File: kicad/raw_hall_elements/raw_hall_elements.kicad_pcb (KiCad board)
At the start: 2 copper layers, 23 parts, among them J1 Conn_01x03_Socket, J2 Conn_01x02_Socket, U1 MCP6022

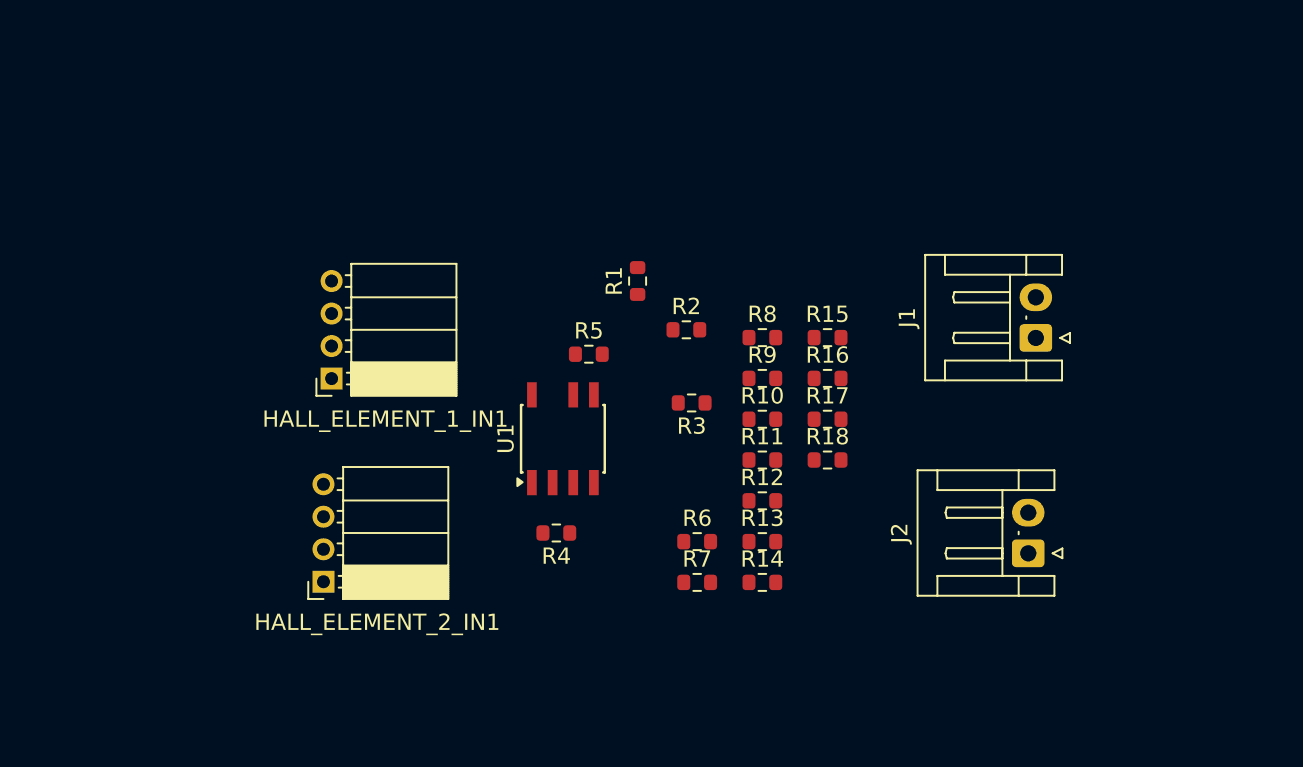
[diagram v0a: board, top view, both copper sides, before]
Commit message: Schematic now uses smaller opamp
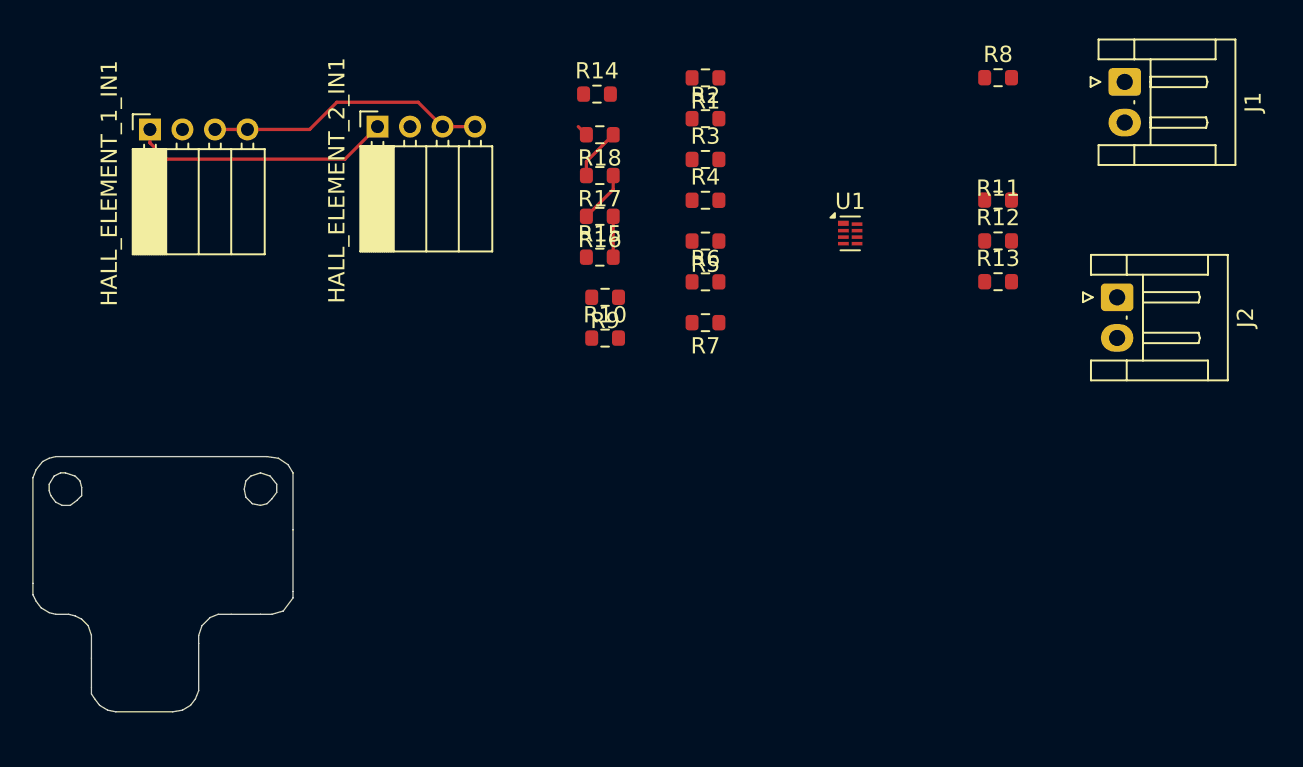
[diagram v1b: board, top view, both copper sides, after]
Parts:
- U1: value MCP6022 -> LMV358; footprint Package_SO:SOIC-8-N7_3.9x4.9mm_P1.27mm -> Package_DFN_QFN:OnSemi_UDFN-8_1.2x1.8mm_P0.4mm
- moved R14 31.7 mm to (136.0, 49.5)
- moved HALL_ELEMENT_2_IN1 28.2 mm to (122.5, 51.5), turned to 90 degrees
- moved R18 24.4 mm to (136.2, 52.0), turned to 180 degrees
- moved R4 22.4 mm to (142.7, 56.0), turned to 0 degrees
- moved U1 21.7 mm to (151.6, 58.1), turned to 0 degrees
- moved R11 21.6 mm to (160.7, 56.0)
- moved R13 21.6 mm to (160.7, 61.0)
- moved R8 21.6 mm to (160.7, 48.5)
- moved R12 21.6 mm to (160.7, 58.5)
- moved R17 20.5 mm to (136.2, 54.5), turned to 180 degrees
- moved HALL_ELEMENT_1_IN1 19.0 mm to (108.5, 51.7), turned to 90 degrees
- moved R16 17.2 mm to (136.2, 57.0), turned to 180 degrees
- moved J1 16.7 mm to (168.5, 48.8), turned to -90 degrees
- moved J2 16.7 mm to (168.0, 62.0), turned to -90 degrees
- moved R6 16.0 mm to (142.7, 61.0)
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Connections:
- R13 pad 1: Net-(R13-Pad1) -> Hall1_out+
- R16 pad 1: Net-(R15-Pad2) -> Hall2_out+
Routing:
- net Vin-: track 0.00 -> 18.0 mm
- net Vin+: track 0.00 -> 16.1 mm
- net Hall2_adj+: track 0.00 -> 3.19 mm
- net Net-(R17-Pad2): track 0.00 -> 3.19 mm
- net Net-(R15-Pad2): track 0.00 -> 2.51 mm
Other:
- board outline added: 16 x 15.7 mm
- board text added: "For Instructional Use Only."
- board text added: "SOLIDWORKS Educational Product."

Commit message: more progress
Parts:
- removed HALL_ELEMENT_1_IN1, HALL_ELEMENT_2_IN1: Conn_01x04, Connector_PinSocket_2.00mm:PinSocket_1x04_P2.00mm_Horizontal
- removed J1: Conn_01x03_Socket, Connector_JST:JST_EH_S2B-EH_1x02_P2.50mm_Horizontal
- removed J2: Conn_01x02_Socket, Connector_JST:JST_EH_S2B-EH_1x02_P2.50mm_Horizontal
- removed R12, R18: 1.5k, Resistor_SMD:R_0603_1608Metric
- removed R14, R15: 200, Resistor_SMD:R_0603_1608Metric
- added 3V3: Conn_01x01, TestPoint:TestPoint_THTPad_1.0x1.0mm_Drill0.5mm, F.Cu at (105.5, 73.0)
- added 5V1: Conn_01x01, TestPoint:TestPoint_THTPad_1.0x1.0mm_Drill0.5mm, F.Cu at (107.5, 73.0)
- added GND1: Conn_01x01, TestPoint:TestPoint_THTPad_1.0x1.0mm_Drill0.5mm, F.Cu at (109.5, 73.0)
- added IC1: AHE300G-PA4-B, KiCad:AHE300GPA4B, F.Cu at (103.0, 80.2)
- added IC2: AHE300G-PA4-B, KiCad:AHE300GPA4B, F.Cu at (112.5, 80.0)
- added VO1: Conn_01x01, TestPoint:TestPoint_THTPad_1.0x1.0mm_Drill0.5mm, F.Cu at (106.0, 86.5)
- added VO2: Conn_01x01, TestPoint:TestPoint_THTPad_1.0x1.0mm_Drill0.5mm, F.Cu at (110.0, 86.5)
- moved R8 61.6 mm to (105.8, 76.5)
- moved R13 54.7 mm to (109.2, 79.5)
- moved R11 49.5 mm to (115.2, 75.5)
- moved U1 46.8 mm to (108.9, 77.4), turned to 90 degrees
- moved R3 42.5 mm to (106.0, 75.0)
- moved R6 42.4 mm to (102.8, 75.5)
- moved R7 42.1 mm to (102.8, 77.0), turned to 0 degrees
- moved R17 41.6 mm to (106.3, 83.5), turned to 0 degrees
- moved R1 38.8 mm to (112.2, 72.5), turned to 0 degrees
- moved R4 38.4 mm to (109.3, 75.0)
- moved R2 38.2 mm to (112.2, 74.0)
- moved R16 37.4 mm to (109.8, 83.5), turned to 0 degrees
- moved R5 34.8 mm to (112.3, 75.5), turned to 0 degrees
- moved R9 28.5 mm to (112.3, 77.0), turned to 0 degrees
- moved R10 24.6 mm to (115.3, 77.0)
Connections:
- R11 pad 2: Net-(R11-Pad2) -> Vin-
- R17 pad 2: Net-(R17-Pad2) -> Vin-
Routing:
- net Vin-: track 18.0 -> 0.00 mm
- net Vin+: track 16.1 -> 0.00 mm
- net Hall2_adj+: track 3.19 -> 0.00 mm
- net Net-(R17-Pad2): track 3.19 -> 0.00 mm
- net Net-(R15-Pad2): track 2.51 -> 0.00 mm

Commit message: more progress 2
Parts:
- moved VO1 35.5 mm to (138.0, 71.1)
- moved R7 32.9 mm to (135.3, 71.8), turned to 90 degrees
- moved R17 31.3 mm to (137.1, 77.5)
- moved R6 31.1 mm to (133.3, 81.7)
- moved VO2 31.0 mm to (138.0, 73.1)
- moved R4 28.6 mm to (137.1, 81.8)
- moved R16 27.5 mm to (137.1, 79.7)
- moved R3 27.2 mm to (133.0, 71.8), turned to 90 degrees
- moved IC1 26.6 mm to (128.6, 87.5), turned to 90 degrees
- moved R13 24.4 mm to (133.5, 78.1), turned to 90 degrees
- moved R8 22.2 mm to (127.9, 74.1)
- moved U1 22.0 mm to (130.9, 76.9)
- moved IC2 20.8 mm to (131.9, 87.5), turned to 90 degrees
- moved GND1 20.6 mm to (130.0, 71.2)
- moved R1 20.4 mm to (132.5, 74.7)
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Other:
- board size 16 x 15.7 mm -> 16 x 19.1 mm

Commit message: one more trace ahhhhh
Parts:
- removed U1: LMV358, Package_DFN_QFN:OnSemi_UDFN-8_1.2x1.8mm_P0.4mm
- added U2: MCP6002-xMS, Package_SO:MSOP-8_3x3mm_P0.65mm, F.Cu at (130.9, 77.1)
- moved R1 3.28 mm to (131.0, 71.8), turned to 90 degrees
- moved GND1 1.60 mm to (128.4, 71.2)
- moved R2 1.41 mm to (128.3, 81.9)
- moved R11 0.92 mm to (127.8, 78.7)
- moved R16 0.85 mm to (136.6, 79.0)
- moved R8 0.81 mm to (127.5, 74.8), turned to 90 degrees
- moved 5V1 0.80 mm to (126.4, 71.2)
- moved R13 0.78 mm to (134.0, 78.7)
- moved VO2 0.60 mm to (137.4, 73.1)
- moved R17 0.52 mm to (136.6, 77.3)
- moved VO1 0.50 mm to (137.5, 71.1)
- moved R5 0.44 mm to (125.3, 77.7)
- moved R10 0.34 mm to (125.3, 79.5)
- moved IC1 0.22 mm to (128.7, 87.7)
- moved IC2 0.22 mm to (132.0, 87.7)
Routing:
- net Vin-: track 0.00 -> 44.1 mm, vias 0 -> 3
- net Vout1: track 0.00 -> 21.7 mm
- net Hall2_adj+: track 0.00 -> 21.3 mm, vias 0 -> 4
- net +1V65: track 0.00 -> 20.6 mm, vias 0 -> 6
- net +3V3: track 0.00 -> 18.3 mm
- net Net-(U2A-+): track 0.00 -> 18.2 mm, vias 0 -> 2
- net Vin+: track 0.00 -> 15.5 mm, vias 0 -> 1
- net Hall1_adj+: track 0.00 -> 14.1 mm, vias 0 -> 2
- net Net-(U2B-+): track 0.00 -> 12.8 mm, vias 0 -> 2
- net Hall2_out+: track 0.00 -> 12.2 mm, vias 0 -> 1
- net +5V: track 0.00 -> 11.8 mm
- net Vout2: track 0.00 -> 11.7 mm
- net Net-(U2B--): track 0.00 -> 11.2 mm, vias 0 -> 2
- net Net-(U2A--): track 0.00 -> 3.51 mm

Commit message: schematic clean up and layout finalise
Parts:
- 3V3, 5V1, GND1, VO1, VO2: footprint TestPoint:TestPoint_THTPad_1.0x1.0mm_Drill0.5mm -> TestPoint:TestPoint_THTPad_1.5x1.5mm_Drill0.7mm
- moved R7 0.64 mm to (134.7, 71.8)
- moved VO1 0.45 mm to (137.2, 70.8)
- moved GND1 0.44 mm to (128.8, 71.4)
- moved VO2 0.35 mm to (137.1, 72.9)
- moved 3V3 0.28 mm to (124.3, 71.5)
- moved 5V1 0.28 mm to (126.5, 71.5)
- moved IC1 0.27 mm to (128.7, 87.4)
- moved IC2 0.27 mm to (132.0, 87.4)
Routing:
- net Hall1_out+: track 0.00 -> 14.4 mm, vias 0 -> 3
- net Vin-: track 44.1 -> 47.9 mm
- net +1V65: track 20.6 -> 20.0 mm
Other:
- board text removed: "For Instructional Use Only."
- board text removed: "SOLIDWORKS Educational Product."

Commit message: clean up schematic, finish layout and sent for manuf
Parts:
- added G***: LOGO, LOGO, B.Cu at (130.1, 77.7)
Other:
- board text added: "Alex SSL26"
- board text added: "HALL EXP"
- board text added: "JLCJLCJLCJLC"
